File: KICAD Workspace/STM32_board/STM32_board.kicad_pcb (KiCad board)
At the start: 2 copper layers, 154.9 x 133.4 mm, 16 parts, among them J1 Power connector, J2 High side connector, J3 Sensors connector, J4 LCD interface, J5 Low side connector, J6 3v3_out, U1 CD4050BE, U2 LM7805_TO220, U3 LP2950-3.3_TO92

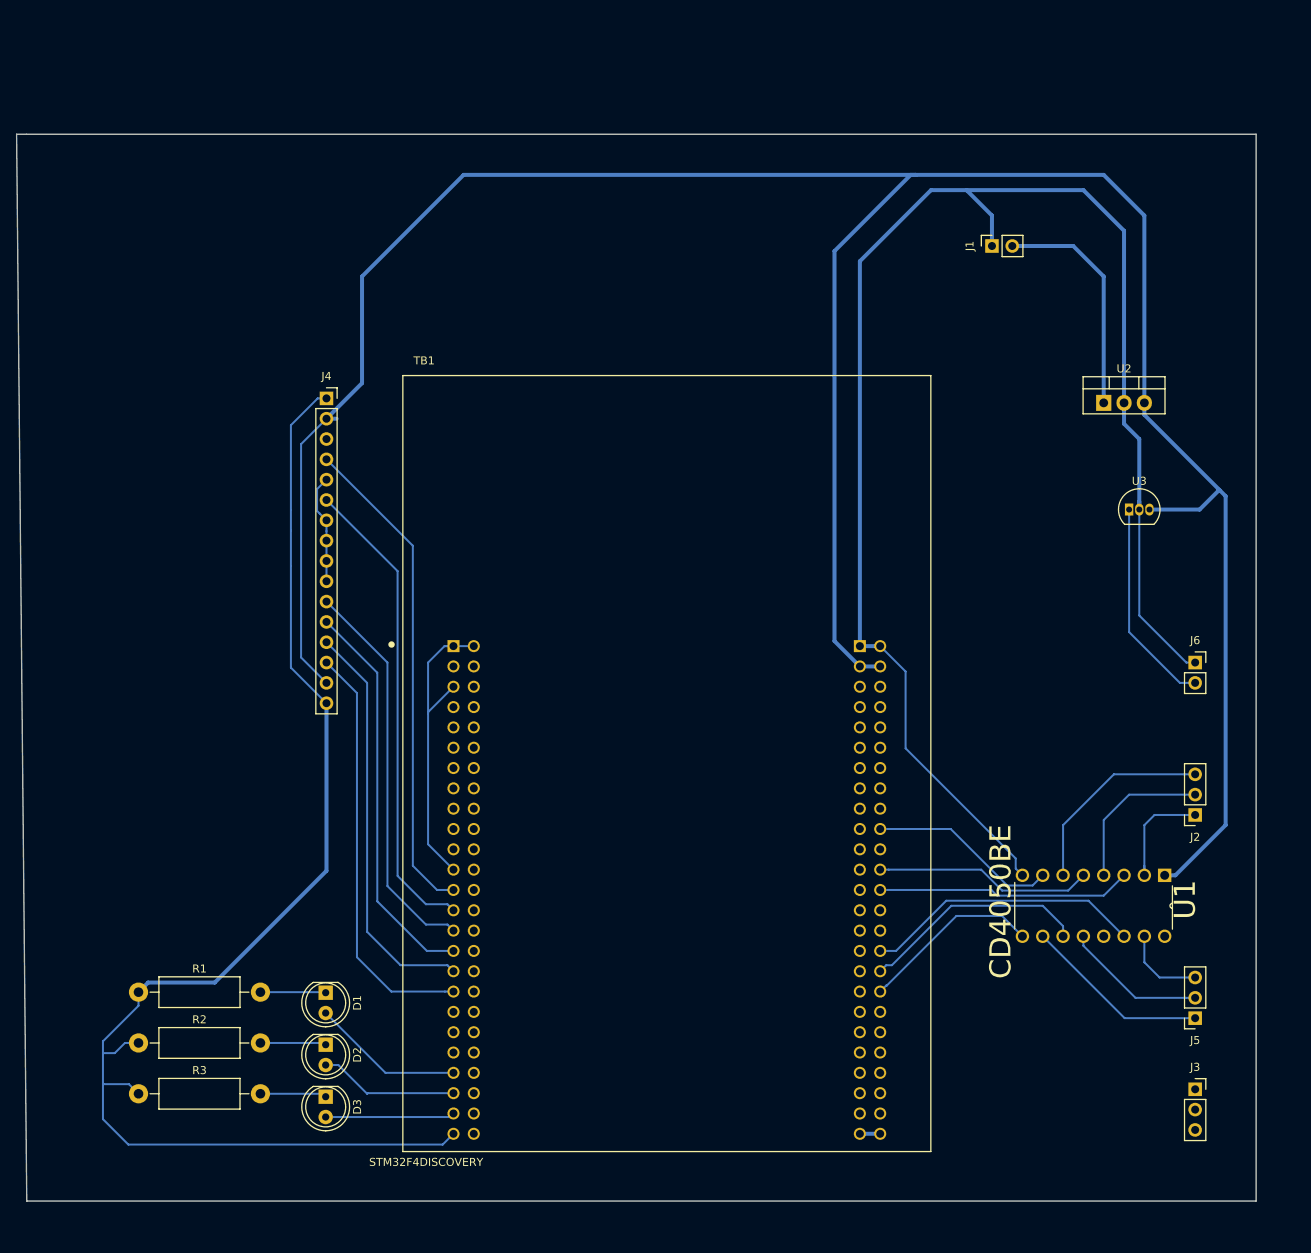
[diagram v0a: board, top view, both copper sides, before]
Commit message: Added some footprints and conenctors
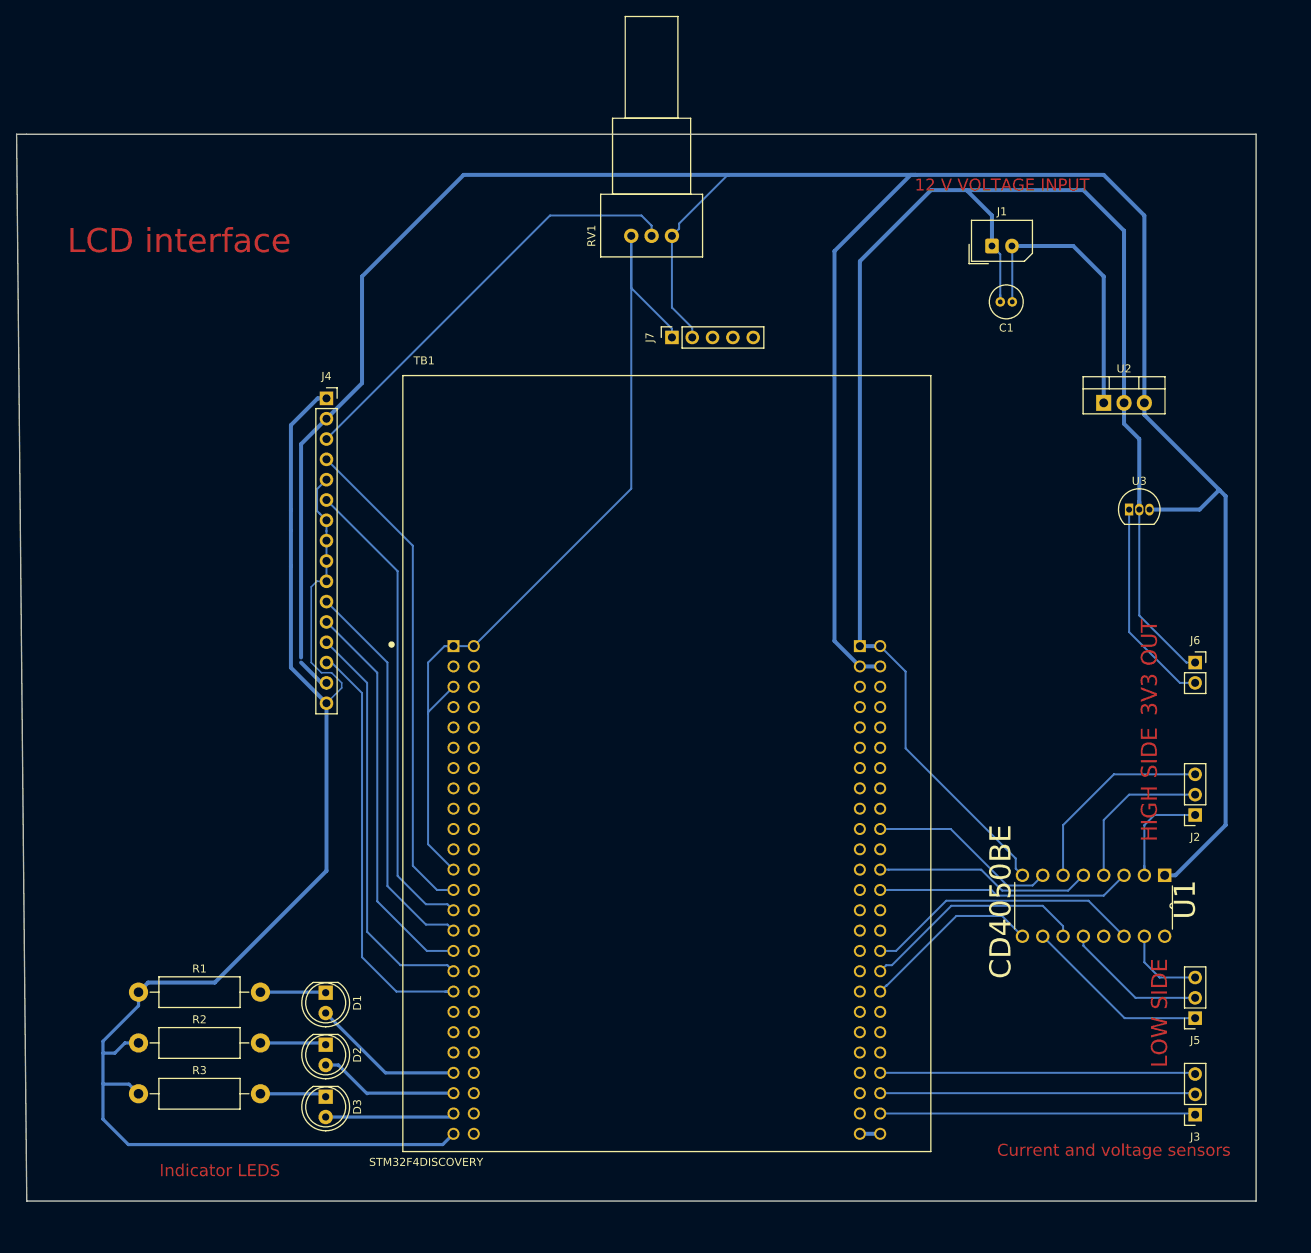
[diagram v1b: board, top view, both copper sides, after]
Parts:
- added C1: CP, Capacitor_THT:C_Radial_D4.0mm_H7.0mm_P1.50mm, F.Cu at (174.0, 47.6)
- added J7: Joystick connector, Connector_PinSocket_2.54mm:PinSocket_1x05_P2.54mm_Vertical, F.Cu at (131.4, 52.1)
- added RV1: R_POT, Potentiometer_THT:Potentiometer_Vishay_248GJ-249GJ_Single_Horizontal, F.Cu at (131.4, 39.4)
- J1: footprint Connector_PinSocket_2.54mm:PinSocket_1x02_P2.54mm_Vertical -> Connector_Molex:Molex_SPOX_5267-02A_1x02_P2.50mm_Vertical
- moved J3 3.17 mm to (196.8, 149.2), turned to 180 degrees
- turned J1 to 0 degrees
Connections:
- J3 pad 1: /CURRENT_SENSOR -> /ADC_BATTERY
- J3 pad 2: /ADC_BATTERY -> /CURRENT_SENSOR
- TB1 pad P2_44: Net-(TB1-PadP2_44) -> /READ_BATTERY
- TB1 pad P2_46: Net-(TB1-PadP2_46) -> /CURRENT_SENSOR
- TB1 pad P2_48: Net-(TB1-PadP2_48) -> /ADC_BATTERY
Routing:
- net /GND: track 415.2 -> 518.1 mm
- net /V0: track 0.00 -> 54.0 mm
- net /READ_BATTERY: track 0.00 -> 39.4 mm
- net /CURRENT_SENSOR: track 0.00 -> 39.4 mm
- net /ADC_BATTERY: track 0.00 -> 39.4 mm
- net /5V: track 332.2 -> 355.2 mm
- net /12V: track 28.8 -> 35.8 mm
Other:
- board text added: "12 V VOLTAGE INPUT"
- board text added: "3V3 OUT"
- board text added: "Current and voltage sensors"
- board text added: "HIGH SIDE"
- board text added: "Indicator LEDS"
- board text added: "LCD interface"
- board text added: "LOW SIDE"

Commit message: Added some footprints.
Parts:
- added C2: C, Capacitor_THT:CP_Radial_D5.0mm_P2.50mm, F.Cu at (199.4, 66.7)
- added C3: C3, Capacitor_THT:CP_Radial_D5.0mm_P2.50mm, F.Cu at (200.0, 81.3)
- added C4: C4, Capacitor_THT:CP_Radial_D5.0mm_P2.50mm, F.Cu at (184.8, 74.3)
- RV1: footprint Potentiometer_THT:Potentiometer_Vishay_248GJ-249GJ_Single_Horizontal -> Potentiometer_THT:Potentiometer_Alps_RK163_Single_Horizontal
- moved J7 8.28 mm to (139.7, 51.4)
- moved RV1 8.25 mm to (139.7, 39.4)
- moved D1 3.18 mm to (91.3, 134.0)
- moved D2 3.18 mm to (91.3, 140.5)
- moved D3 3.18 mm to (91.3, 147.0)
- moved J1 3.18 mm to (174.6, 40.6)
- moved J2 3.18 mm to (200.0, 111.8)
- moved J3 3.18 mm to (200.0, 149.2)
- moved J5 3.18 mm to (200.0, 137.2)
- moved J6 3.18 mm to (200.0, 92.7)
- moved TB1 3.18 mm to (134.0, 105.3)
- moved U1 3.18 mm to (178.4, 126.9)
- moved U2 3.18 mm to (188.6, 60.2)
- moved U3 3.18 mm to (191.8, 73.6)
- moved J4 3.17 mm to (91.4, 59.7)
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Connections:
- J7 pad 3: Net-(J7-Pad3) -> /JoystickADC1
- J7 pad 4: Net-(J7-Pad4) -> /JoystickADC2
- J7 pad 5: Net-(J7-Pad5) -> /JoystickButton
- TB1 pad P1_10: Net-(TB1-PadP1_10) -> /JoystickADC2
- TB1 pad P1_11: /JoystickButton -> Net-(TB1-PadP1_11)
- TB1 pad P1_14: Net-(TB1-PadP1_14) -> /JoystickButton
- TB1 pad P1_7: /JoystickADC1 -> Net-(TB1-PadP1_7)
- TB1 pad P1_8: Net-(TB1-PadP1_8) -> /JoystickADC1
- TB1 pad P1_9: /JoystickADC2 -> Net-(TB1-PadP1_9)
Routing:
- net /JoystickADC2: track 0.00 -> 88.7 mm
- net /5V: track 355.2 -> 436.4 mm
- net /JoystickButton: track 0.00 -> 76.4 mm
- net /JoystickADC1: track 0.00 -> 64.0 mm
- net Net-(TB1-PadP1_18): track 0.00 -> 56.9 mm
- net /GND: track 518.1 -> 572.5 mm
- net Net-(TB1-PadP1_20): track 0.00 -> 53.9 mm
- net Net-(TB1-PadP1_22): track 0.00 -> 50.2 mm
- net Net-(TB1-PadP1_24): track 0.00 -> 46.7 mm
- net Net-(TB1-PadP1_26): track 0.00 -> 42.4 mm
- net Net-(TB1-PadP1_28): track 0.00 -> 37.7 mm
- net Net-(TB1-PadP1_30): track 0.00 -> 31.7 mm
- net Net-(TB1-PadP2_37): track 0.00 -> 25.4 mm
- net Net-(TB1-PadP2_38): track 0.00 -> 25.2 mm
- net /3V3: track 26.2 -> 33.5 mm
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- added copper zone on B.Cu, net /GND
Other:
- board size 154.9 x 133.4 mm -> 154.9 x 139.1 mm
- board text added: "SENSORLESS MOTOR CONTROLLER"
